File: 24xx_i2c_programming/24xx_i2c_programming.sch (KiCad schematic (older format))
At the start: 11 parts, among them J1 EXPANSION_BOTTOM, J2 A0, J3 A1, J4 A2, J5 WP, U1 24LC00

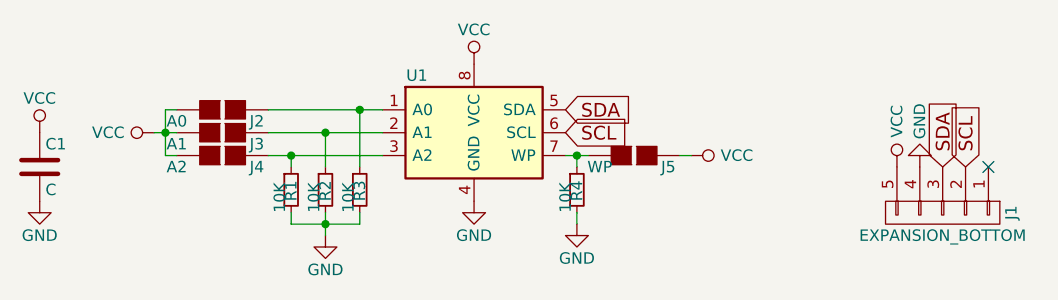
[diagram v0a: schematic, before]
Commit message: Updating I2C pinout in 24xx EEPROM board
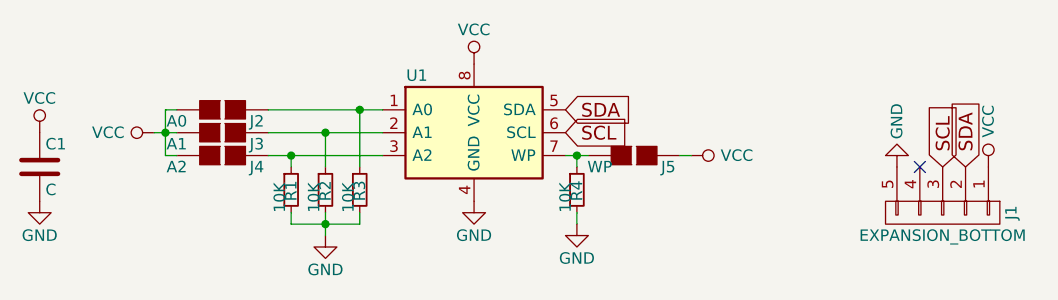
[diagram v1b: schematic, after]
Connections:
- net GND: now also J1.5 (P5); no longer J1.4 (P4)
- net SCL: now also J1.3 (P3); no longer J1.2 (P2)
- net SDA: now also J1.2 (P2); no longer J1.3 (P3)
- net VCC: now also J1.1 (P1); no longer J1.5 (P5)
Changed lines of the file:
@@
 L GND #PWR05
 U 1 1 5960AD91
-P 7450 4150
-F 0 "#PWR05" H 7450 3900 50  0001 C CNN
-F 1 "GND" V 7450 3950 50  0000 C CNN
-F 2 "" H 7450 4150 50  0001 C CNN
-F 3 "" H 7450 4150 50  0001 C CNN
-	1    7450 4150
+P 7350 4150
+F 0 "#PWR05" H 7350 3900 50  0001 C CNN
+F 1 "GND" V 7350 3950 50  0000 C CNN
+F 2 "" H 7350 4150 50  0001 C CNN
+F 3 "" H 7350 4150 50  0001 C CNN
+	1    7350 4150
 	-1   0    0    1
 $EndComp
@@
 L VCC #PWR06
 U 1 1 5960ADA5
-P 7350 4150
-F 0 "#PWR06" H 7350 4000 50  0001 C CNN
-F 1 "VCC" V 7350 4350 50  0000 C CNN
-F 2 "" H 7350 4150 50  0001 C CNN
-F 3 "" H 7350 4150 50  0001 C CNN
-	1    7350 4150
+P 7750 4150
+F 0 "#PWR06" H 7750 4000 50  0001 C CNN
+F 1 "VCC" V 7750 4350 50  0000 C CNN
+F 2 "" H 7750 4150 50  0001 C CNN
+F 3 "" H 7750 4150 50  0001 C CNN
+	1    7750 4150
 	1    0    0    -1
 $EndComp
+Text GLabel 7550 4150 1    60   Input ~ 0
+SCL
 Text GLabel 7650 4150 1    60   Input ~ 0
-SCL
-Text GLabel 7550 4150 1    60   Input ~ 0
 SDA
-NoConn ~ 7750 4150
+NoConn ~ 7450 4150
 $Comp
 L 24LC00 U1
